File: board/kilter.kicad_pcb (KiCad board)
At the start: 2 copper layers, 30.5 x 110 mm, 130 parts, among them J1 IN1, J10 CV2, J2 HP, J3 IN2, J4 LP, J5 BP, J6 POWER, J7 NOTCH, J8 QCV, J9 CV1, Q1 BC858, Q3 BC858, U1 TL074, U10 TL072, U2 TL072, U3 TL074, U4 LM4040C5, U5 TL074, U6 LM13700, U7 LM13700, U8 TL072, U9 TL072

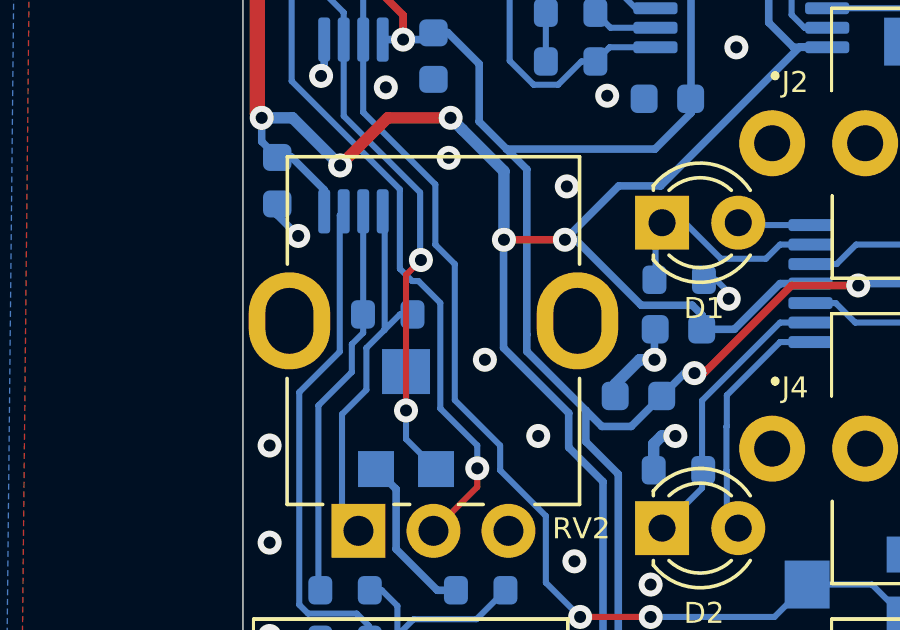
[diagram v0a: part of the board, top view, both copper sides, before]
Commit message: Update panel and add jlcpcb assembly files
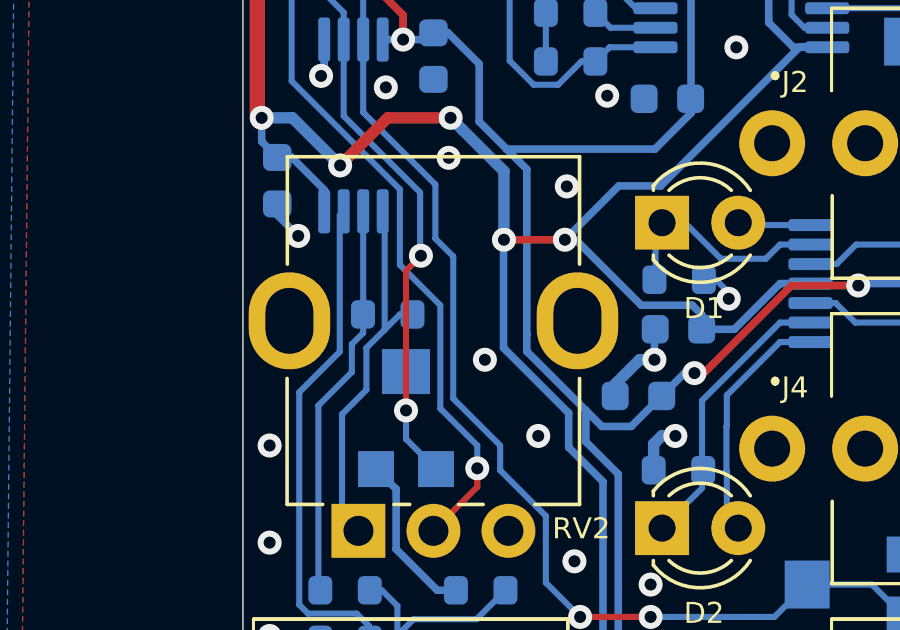
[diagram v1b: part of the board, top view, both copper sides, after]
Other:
- board text added: "TRANS RIGHTS"
- board text added: "ctrx.dev/kilter/v1.0.1"
- board text removed: "github.com/covertneko/kilter /tree/v1.0.0"

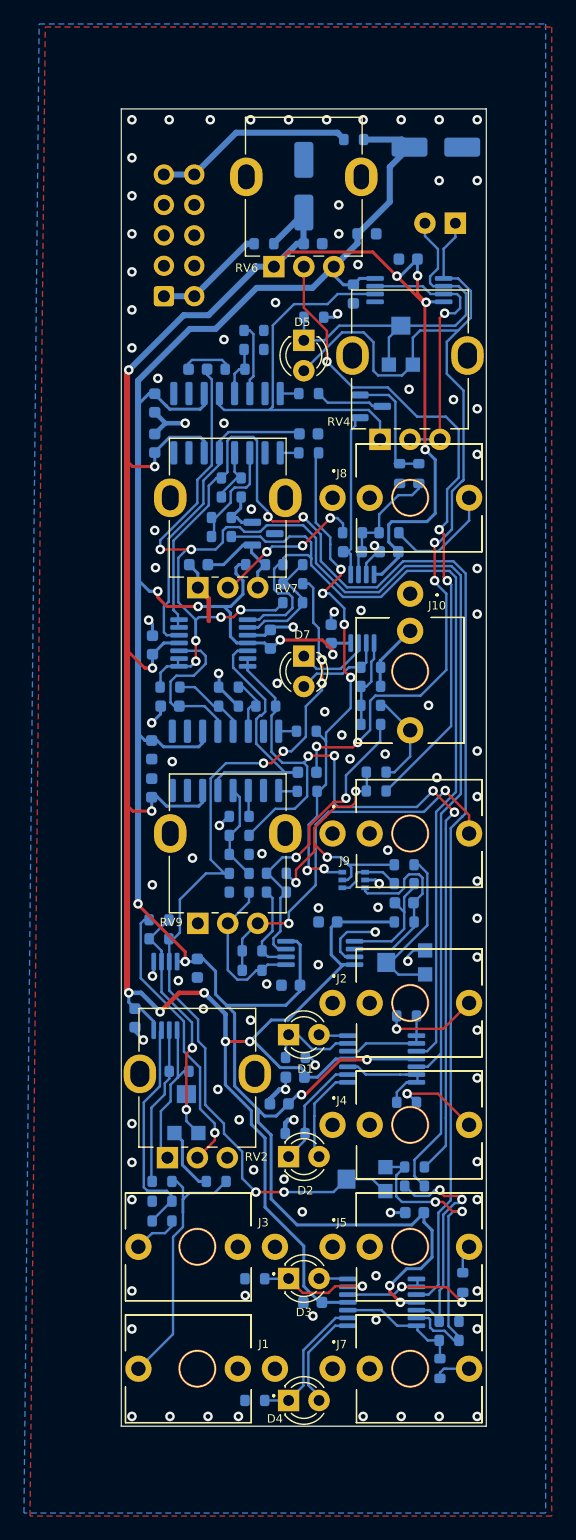
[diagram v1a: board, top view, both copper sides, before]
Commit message: fix resonance gain and simplify module calibration
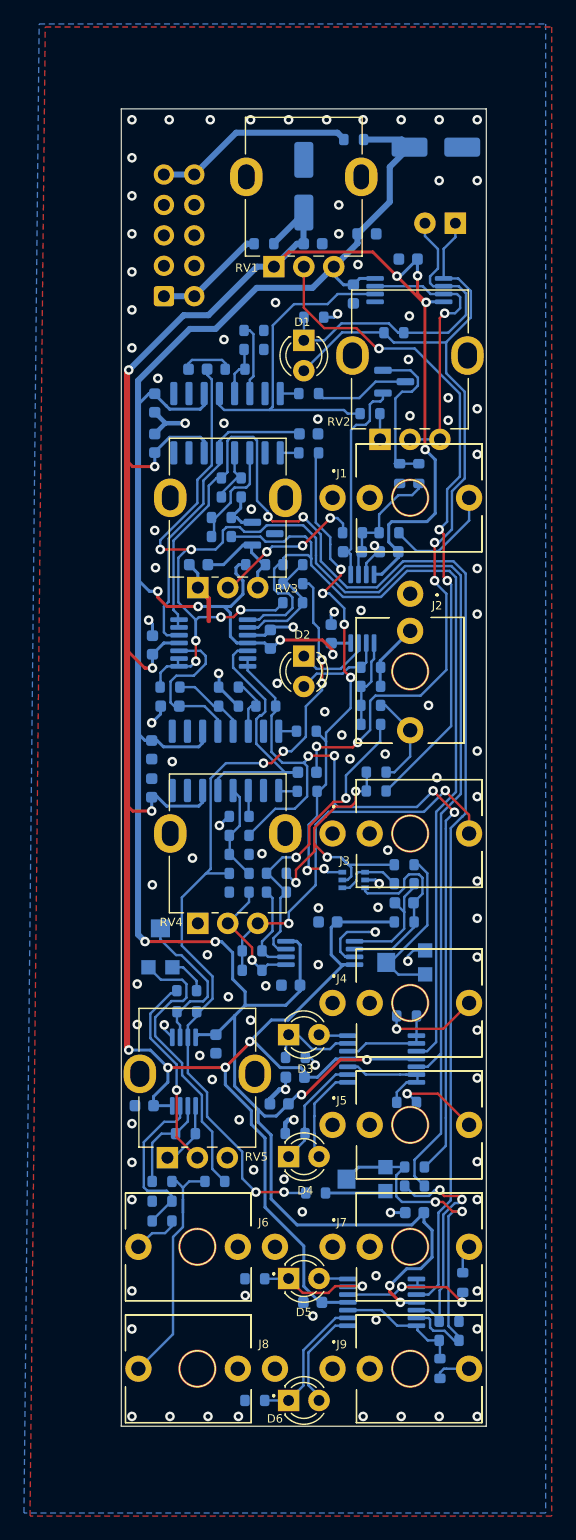
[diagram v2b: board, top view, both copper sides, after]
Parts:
- removed the RV1 at (5.44, 93.6)
- removed the RV5 at (23.3, 29.4)
- added R1: 15K, Resistor_SMD:R_0603_1608Metric, B.Cu at (22.8, 28.6)
- added R56: 10K, Resistor_SMD:R_0603_1608Metric, B.Cu at (16.2, 100.4)
- added R7: 4.7K, Resistor_SMD:R_0603_1608Metric, B.Cu at (20.8, 35.3)
- added RV6: 5K BALANCE, Potentiometer_SMD:Potentiometer_Bourns_TC33X_Vertical, B.Cu at (3.27, 79.8)
- C12: renamed from C27; value 680pF -> 1nF
- Q2: renamed from Q1; value BC858 -> BC857
- R14: renamed from R44; value 100K -> 220K
- R54: renamed from R59; value 47K -> 100K
- RV2: renamed from RV4; value B50K QDRIVE -> B10K QDRIVE
- RV7: renamed from RV8; value 1K TUNE -> 5K TUNE
- RV8: renamed from RV3; value 100K NOTCH DEPTH -> 5K NOTCH
- moved C27 7.37 mm to (1.92, 93.1), turned to 180 degrees
- moved R47 6.51 mm to (5.47, 85.3)
- moved C24 6.51 mm to (7.90, 88.0)
- moved U9 6.51 mm to (5.23, 90.3)
- moved R45 6.35 mm to (5.46, 83.5)
- moved R51 5.23 mm to (5.36, 95.5)
- moved Q1 2.82 mm to (22.8, 32.7)
- moved R54 0.11 mm to (7.81, 99.4), turned to 180 degrees
- renumbered C18 to C10, C22 to C11, C3 to C13, C23 to C14, C16 to C15, C15 to C16, C12 to C17, C29 to C18, C14 to C19, C4 to C2, C28 to C20, C26 to C21, C24 to C22, C25 to C23, C7 to C24, C8 to C25, C9 to C26, C6 to C27, C11 to C28, C10 to C29, C2 to C3, C5 to C4, C20 to C5, C21 to C6, C17 to C7, C19 to C8, C13 to C9, D5 to D1, D7 to D2, D1 to D3, D2 to D4, D3 to D5, D4 to D6, D6 to D7, J8 to J1, J6 to J10, J10 to J2, J9 to J3, J2 to J4, J4 to J5, J3 to J6, J5 to J7, J1 to J8, J7 to J9, Q3 to Q1, R46 to R10, R21 to R11, R32 to R12, R31 to R13, R49 to R15, R28 to R16, R35 to R17, R38 to R18, R13 to R19, R36 to R2, R37 to R20, R55 to R21, R57 to R22, R58 to R23, R29 to R24, R20 to R25, R54 to R26, R23 to R27, R27 to R28, R30 to R29, R42 to R3, R56 to R30, R47 to R31, R25 to R32, R34 to R33, R33 to R34, R22 to R35, R48 to R36, R43 to R37, R51 to R38, R26 to R39, R41 to R4, R53 to R40, R52 to R41, R50 to R42, R60 to R43, R61 to R44, R9 to R45, R4 to R46, R3 to R47, R1 to R48, R10 to R49, R40 to R5, R5 to R50, R2 to R51, R19 to R52, R17 to R53, R6 to R55, R7 to R57, R8 to R58, R12 to R59, R39 to R6, R11 to R60, R15 to R61, R18 to R62, R16 to R63, R14 to R64, R24 to R8, R45 to R9, RV6 to RV1, RV7 to RV3, RV9 to RV4, RV2 to RV5, U8 to U1, U3 to U10, U7 to U2, U4 to U3, U9 to U4, U10 to U7, U1 to U8, U2 to U9
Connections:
- R45 pad 2: Net-(R3-Pad1) -> Net-(R9-Pad2)
- RV8 pad 2: /IN -> Net-(R15-Pad1)
- RV8 pad 3: /IN -> Net-(RV3-Pad3)
- U1 pad 6: Net-(RV4-Pad1) -> Net-(U7-Pad12)
- U2 pad 10: (no net) -> unconnected-(U7-Pad10)
- U2 pad 12: Net-(RV4-Pad1) -> Net-(U7-Pad12)
- U2 pad 7: (no net) -> unconnected-(U7-Pad7)
- U2 pad 8: (no net) -> unconnected-(U7-Pad8)
- U2 pad 9: (no net) -> unconnected-(U7-Pad9)
- U6 pad 10: (no net) -> unconnected-(U6-Pad10)
- U6 pad 7: (no net) -> unconnected-(U6-Pad7)
- U6 pad 8: (no net) -> unconnected-(U6-Pad8)
- U6 pad 9: (no net) -> unconnected-(U6-Pad9)
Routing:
- net Net-(RV4-Pad1): track 33.3 -> 2.15 mm
- net Net-(U7-Pad12): track 0.00 -> 29.8 mm
- net Net-(R59-Pad1): track 5.51 -> 24.3 mm
- net Net-(R3-Pad1): track 21.9 -> 12.9 mm, vias 2 -> 0
- net /IN: track 77.3 -> 69.8 mm
- net Net-(R2-Pad1): track 12.7 -> 5.60 mm
- net Net-(R9-Pad1): track 23.6 -> 16.6 mm
- net Net-(C14-Pad2): track 79.5 -> 73.2 mm
- net Net-(R7-Pad1): track 19.1 -> 14.0 mm
- net Net-(RV3-Pad3): track 0.00 -> 5.07 mm
- net +12V: track 215.6 -> 220.7 mm
- net Net-(R2-Pad2): track 13.3 -> 8.23 mm
- net Net-(C27-Pad1): track 13.9 -> 17.7 mm
- net Net-(R15-Pad1): track 27.0 -> 30.7 mm
- net Net-(R9-Pad2): track 0.00 -> 3.31 mm
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
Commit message: fix back silkscreen and update production files
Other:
- board text added: "catrax.dev/kilter/v1.0.1"
- board text removed: "ctrx.dev/kilter/v1.0.1"
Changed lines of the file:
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@@
   (gr_line (start 0 9.885) (end 0 119.885) (layer "Edge.Cuts") (width 0.05))
   (gr_line (start 0 9.885) (end 30.48 9.885) (layer "Edge.Cuts") (width 0.05))
-  (gr_text "ctrx.dev/kilter/v1.0.1" (at 28.75 56.5785 90) (layer "B.SilkS")
+  (gr_text "catrax.dev/kilter/v1.0.1" (at 28.75 56.5785 90) (layer "B.SilkS")
     (effects (font (size 0.7 0.7) (thickness 0.15)) (justify mirror))
   )
